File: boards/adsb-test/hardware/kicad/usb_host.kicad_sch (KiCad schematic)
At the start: 0 parts

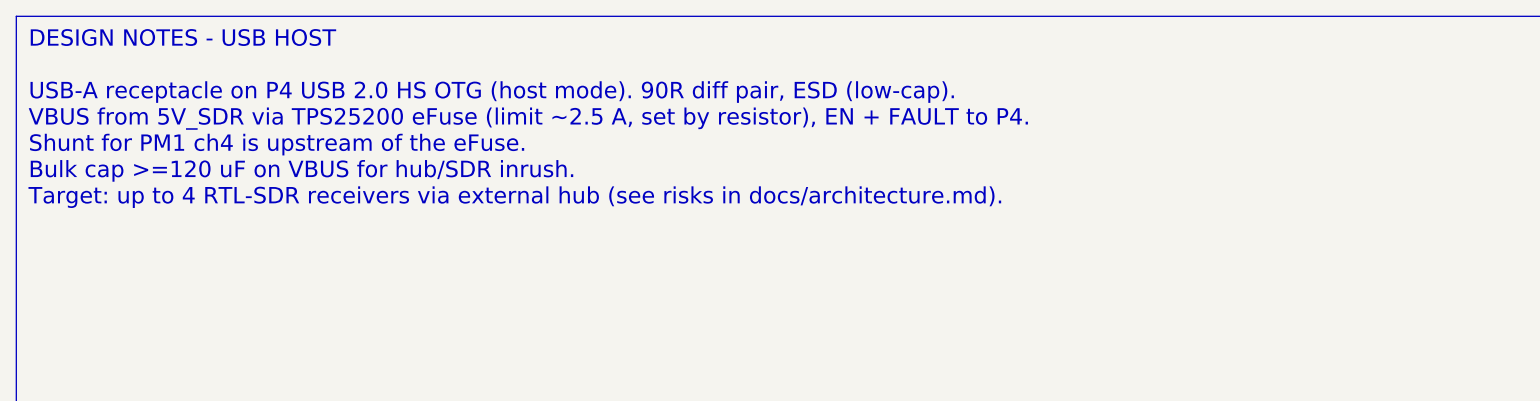
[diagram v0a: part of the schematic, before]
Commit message: Release v0.4.0: ADSB_Test with ESP32-C5, ADSBee m1421 and LA5016 header
- C6 -> C5 co-processor; m1421 identified and integrated (symbol/footprint
  from the ADSBee 1421 carrier, GPL-3.0 attribution)
- Power budget and 2S1P battery sizing for >= 1 h; USB-A for 1-2 SDRs via hub
- Dev port: FT2232H + RP2040 debugprobe; TCA6408A expander for slow I/O
- Test Debug sheet with LA5016 header and rail test points
- Vendor documents git-ignored (public repo)

Co-Authored-By: Claude Opus 5.5 <noreply@anthropic.com>
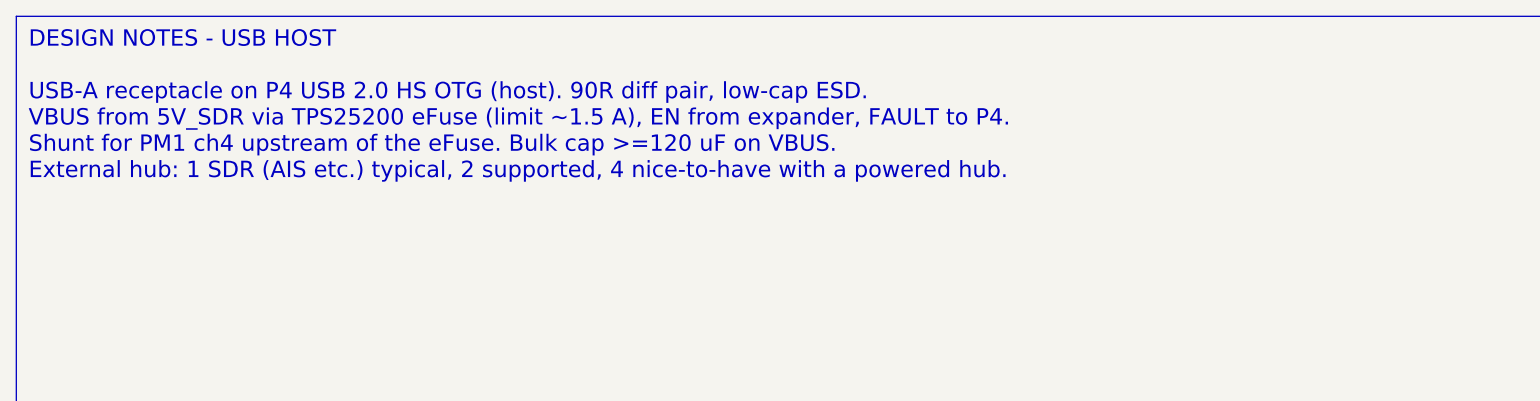
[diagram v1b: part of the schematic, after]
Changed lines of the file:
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@@
 		(comment 1 "Requirements: boards/adsb-test/docs/requirements.md")
 	)
-	(text_box "DESIGN NOTES - USB HOST\n\nUSB-A receptacle on P4 USB 2.0 HS OTG (host mode). 90R diff pair, ESD (low-cap).\nVBUS from 5V_SDR via TPS25200 eFuse (limit ~2.5 A, set by resistor), EN + FAULT to P4.\nShunt for PM1 ch4 is upstream of the eFuse.\nBulk cap >=120 uF on VBUS for hub/SDR inrush.\nTarget: up to 4 RTL-SDR receivers via external hub (see risks in docs/architecture.md)."
+	(text_box "DESIGN NOTES - USB HOST\n\nUSB-A receptacle on P4 USB 2.0 HS OTG (host). 90R diff pair, low-cap ESD.\nVBUS from 5V_SDR via TPS25200 eFuse (limit ~1.5 A), EN from expander, FAULT to P4.\nShunt for PM1 ch4 upstream of the eFuse. Bulk cap >=120 uF on VBUS.\nExternal hub: 1 SDR (AIS etc.) typical, 2 supported, 4 nice-to-have with a powered hub."
 		(exclude_from_sim no)
 		(at 20 20 0)

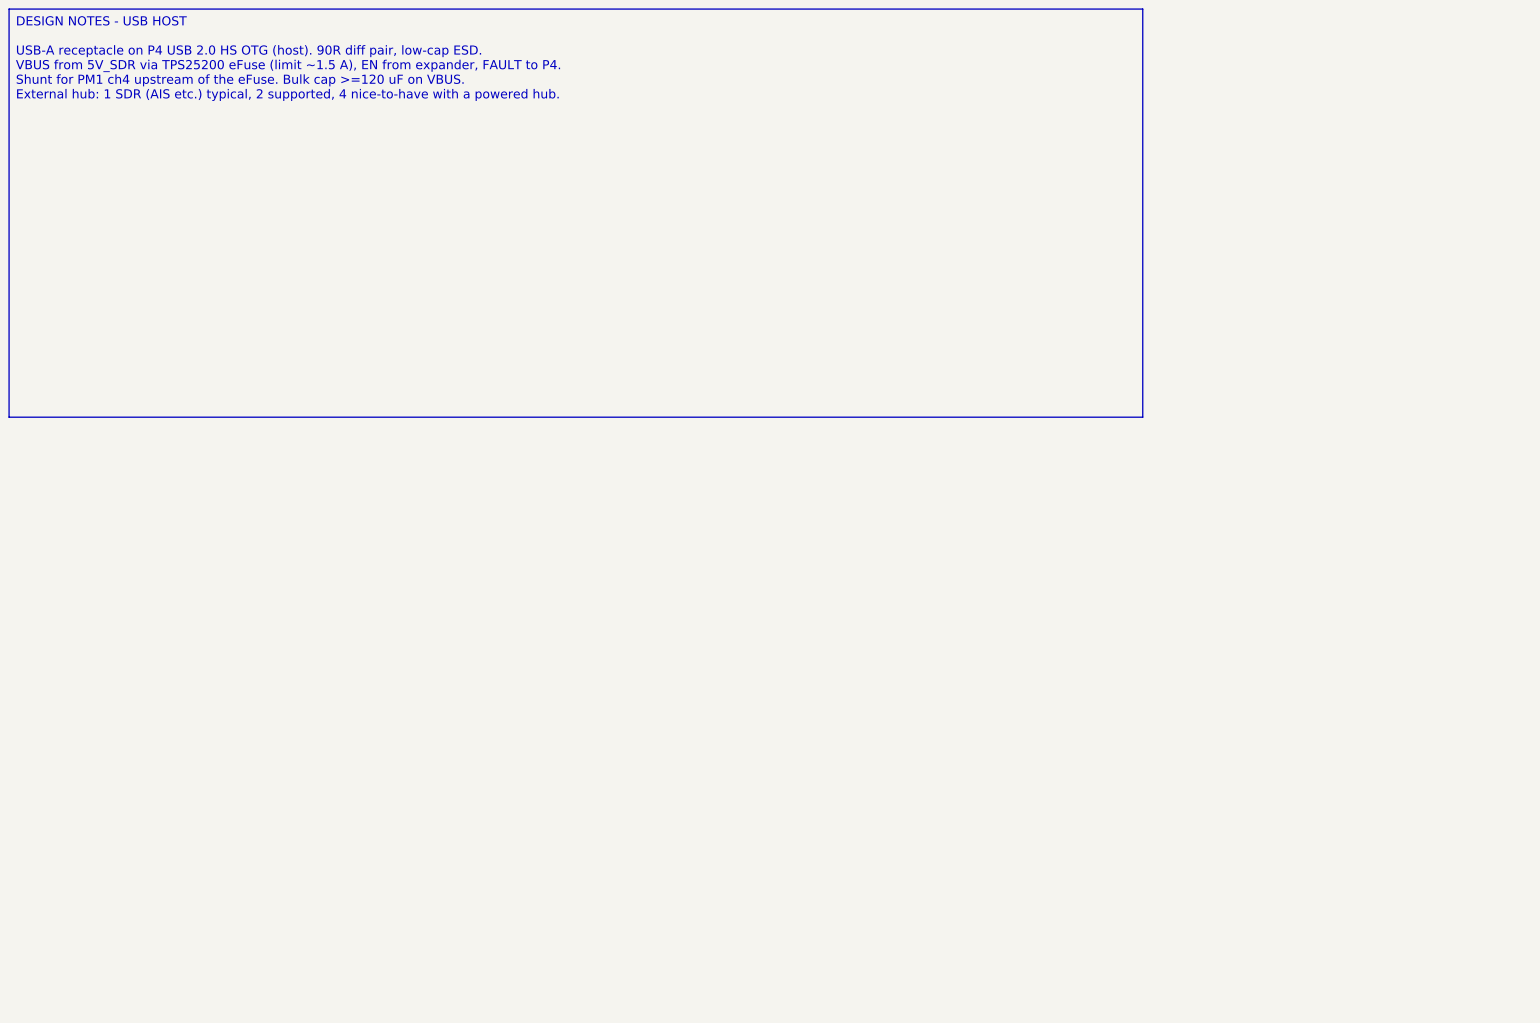
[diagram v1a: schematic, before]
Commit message: Release v0.22.0: all ADSB_Test schematic sheets generated (ERC clean)
Co-Authored-By: Claude Opus 5.5 <noreply@anthropic.com>
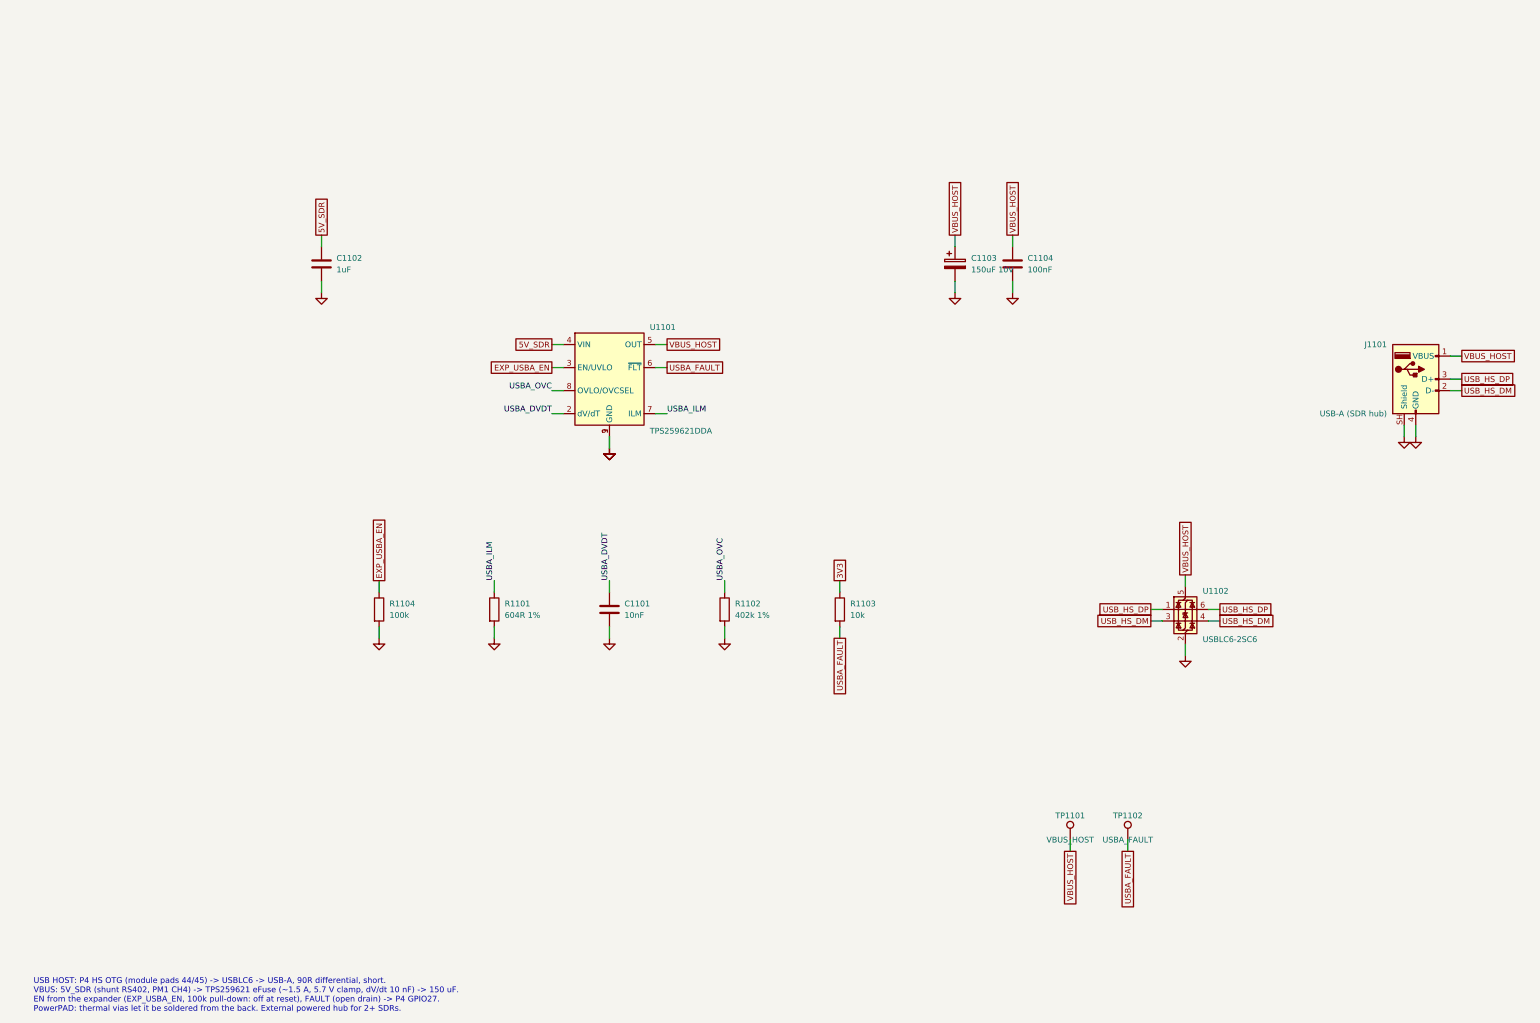
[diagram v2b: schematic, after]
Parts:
- added C1101: 10nF, Capacitor_SMD:C_0805_2012Metric_Pad1.18x1.45mm_HandSolder, symbol Device:C
- added C1102: 1uF, Capacitor_SMD:C_0805_2012Metric_Pad1.18x1.45mm_HandSolder, symbol Device:C
- added C1103: 150uF 10V, Capacitor_SMD:CP_Elec_6.3x5.8, symbol Device:C_Polarized
- added C1104: 100nF, Capacitor_SMD:C_0805_2012Metric_Pad1.18x1.45mm_HandSolder, symbol Device:C
- added J1101: USB-A (SDR hub), Connector_USB:USB_A_Molex_67643_Horizontal, symbol Connector:USB_A
- added R1101: 604R 1%, Resistor_SMD:R_0805_2012Metric_Pad1.20x1.40mm_HandSolder, symbol Device:R
- added R1102: 402k 1%, Resistor_SMD:R_0805_2012Metric_Pad1.20x1.40mm_HandSolder, symbol Device:R
- added R1103: 10k, Resistor_SMD:R_0805_2012Metric_Pad1.20x1.40mm_HandSolder, symbol Device:R
- added R1104: 100k, Resistor_SMD:R_0805_2012Metric_Pad1.20x1.40mm_HandSolder, symbol Device:R
- added TP1101: VBUS_HOST, TestPoint:TestPoint_Pad_D1.5mm, symbol Connector:TestPoint
- added TP1102: USBA_FAULT, TestPoint:TestPoint_Pad_D1.5mm, symbol Connector:TestPoint
- added U1101: TPS259621DDA, Package_SO:TI_SO-PowerPAD-8_ThermalVias, symbol Power_Management:TPS2596xx
- added U1102: USBLC6-2SC6, Package_TO_SOT_SMD:SOT-23-6_Handsoldering, symbol Power_Protection:USBLC6-2SC6
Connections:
- new net 3V3: R1103.1
- new net 5V_SDR: C1102.1, U1101.4 (VIN)
- new net EXP_USBA_EN: R1104.1, U1101.3 (EN/UVLO)
- new net GND: C1101.2, C1102.2, C1103.2, C1104.2, J1101.4 (GND), J1101.SH (Shield), R1101.2, R1102.2, R1104.2, U1101.1 (GND), U1101.9 (GND), U1102.2 (GND)
- new net USBA_DVDT: C1101.1, U1101.2 (dV/dT)
- new net USBA_FAULT: R1103.2, TP1102.1, U1101.6 (~{FLT})
- new net USBA_ILM: R1101.1, U1101.7 (ILM)
- new net USBA_OVC: R1102.1, U1101.8 (OVLO/OVCSEL)
- new net USB_HS_DM: J1101.2 (D-), U1102.3 (I/O2), U1102.4 (I/O2)
- new net USB_HS_DP: J1101.3 (D+), U1102.1 (I/O1), U1102.6 (I/O1)
- new net VBUS_HOST: C1103.1, C1104.1, J1101.1 (VBUS), TP1101.1, U1101.5 (OUT), U1102.5 (VBUS)
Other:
- note added: "USB HOST: P4 HS OTG (module pads 44/45) -> USBLC6 -> USB-A, 90R differential, short. VBUS: 5V_SDR (shunt RS402, PM1 CH4) -> TPS259621 eFuse (~1.5 A, 5.7 V clamp, dV/dt 10 nF) -> 150 uF. EN from the expander (EXP_USBA_EN, 100k pull-down: off at reset), FAULT (open drain) -> P4 GPIO27. PowerPAD: thermal vias let it be soldered from the back. External powered hub for 2+ SDRs."

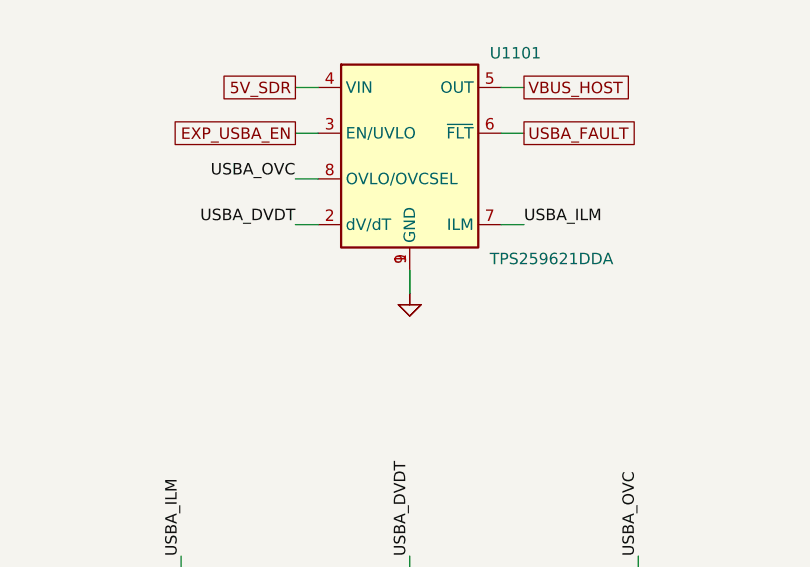
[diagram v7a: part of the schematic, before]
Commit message: Schematic generator: hide stacked pins (KiCad convention) so pin numbers don't overprint
Co-Authored-By: Claude Opus 5.5 <noreply@anthropic.com>
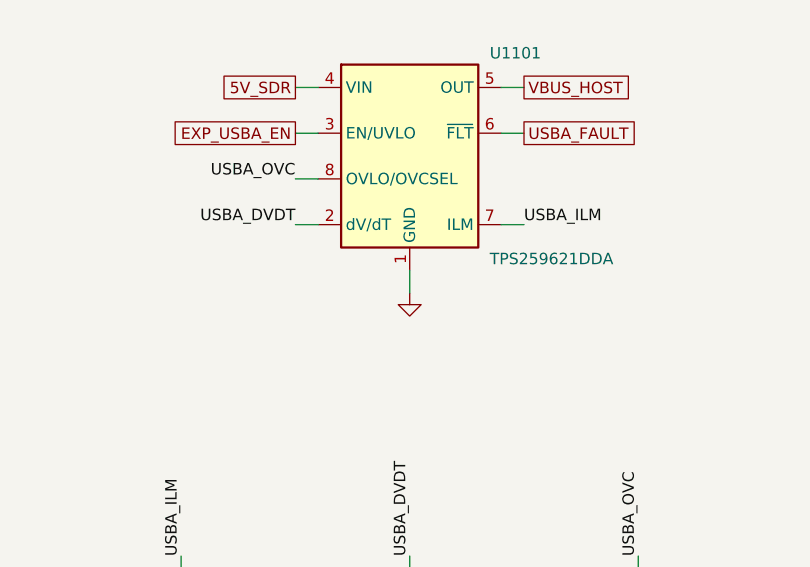
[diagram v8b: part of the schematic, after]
